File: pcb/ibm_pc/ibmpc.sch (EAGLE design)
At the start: 47 parts, among them IC1 STM32F072C8T6, SW1 324_SW, SW2 324_SW, U1 MAX3232

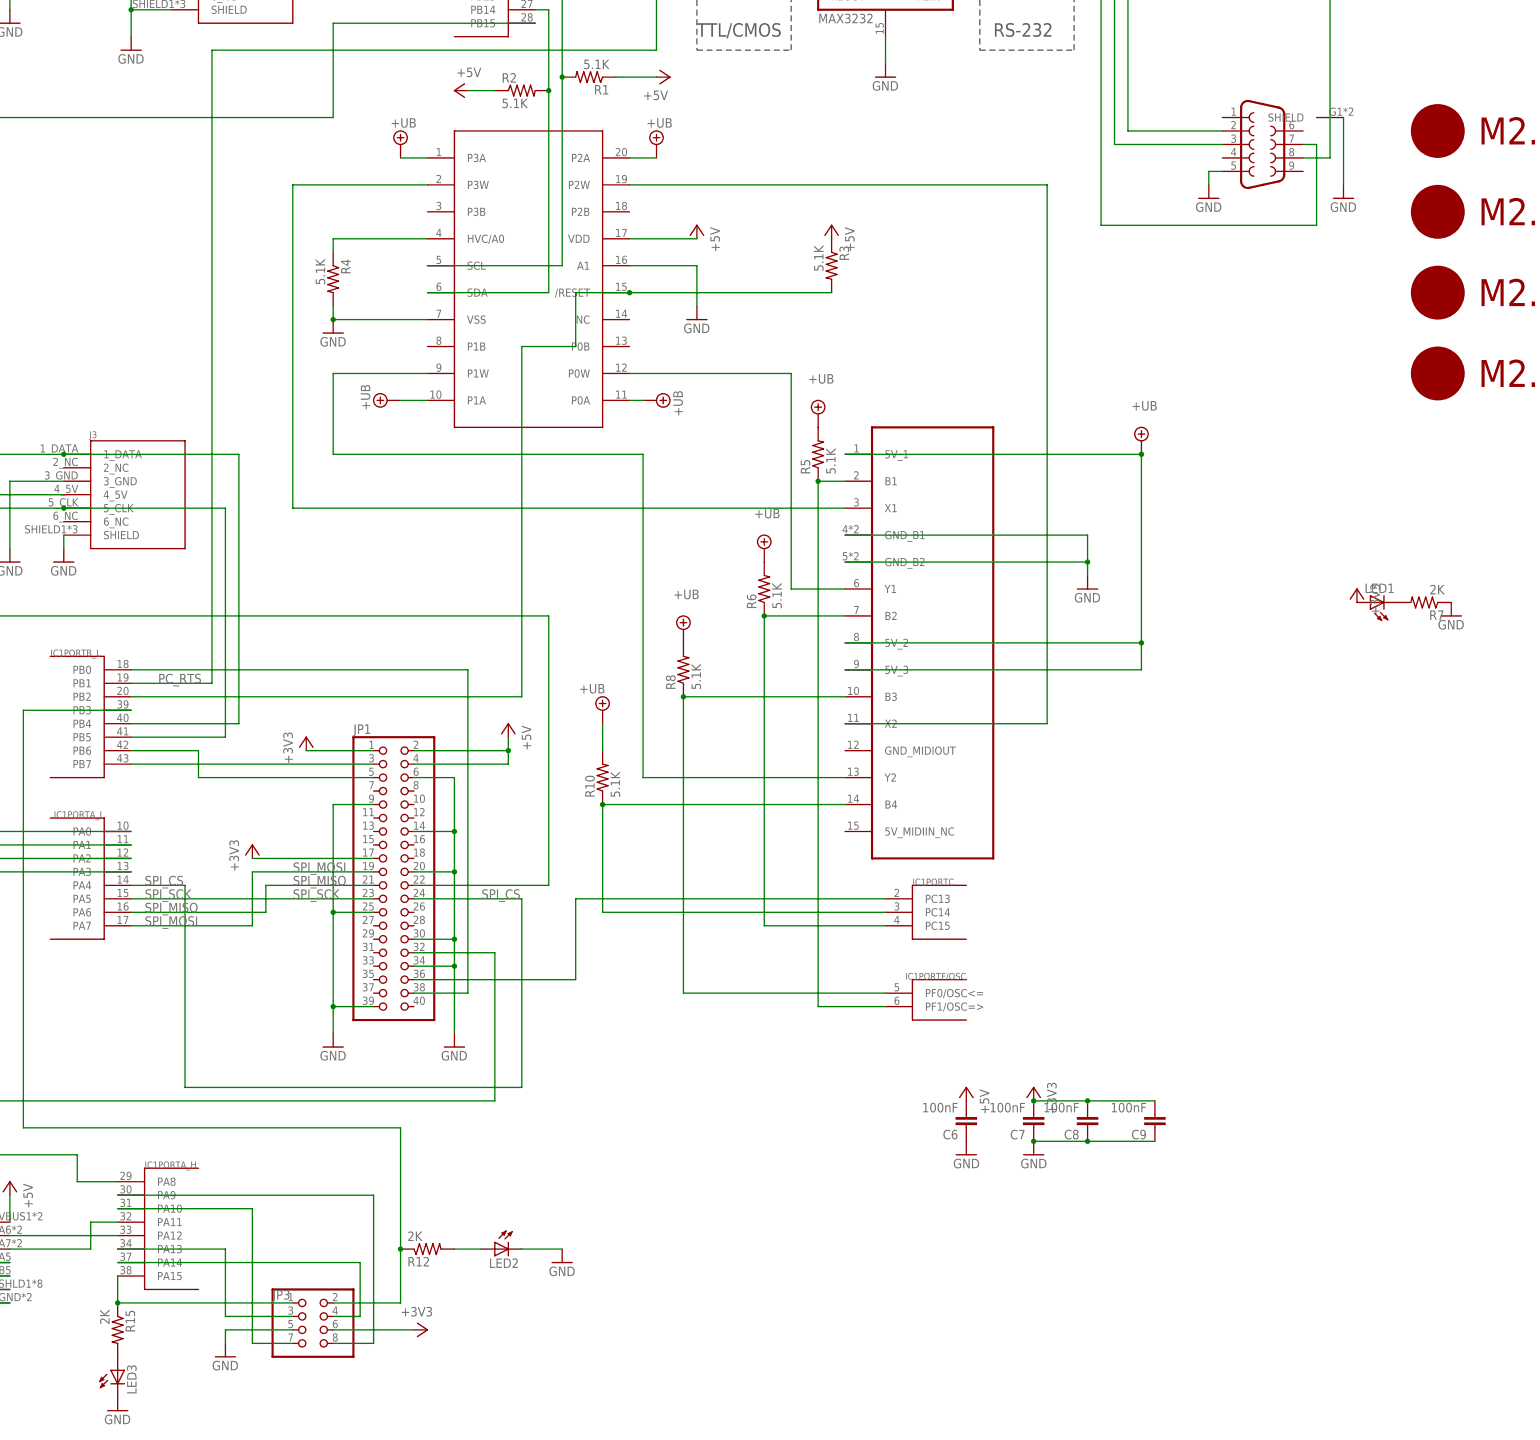
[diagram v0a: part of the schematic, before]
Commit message: added resistor to digipot
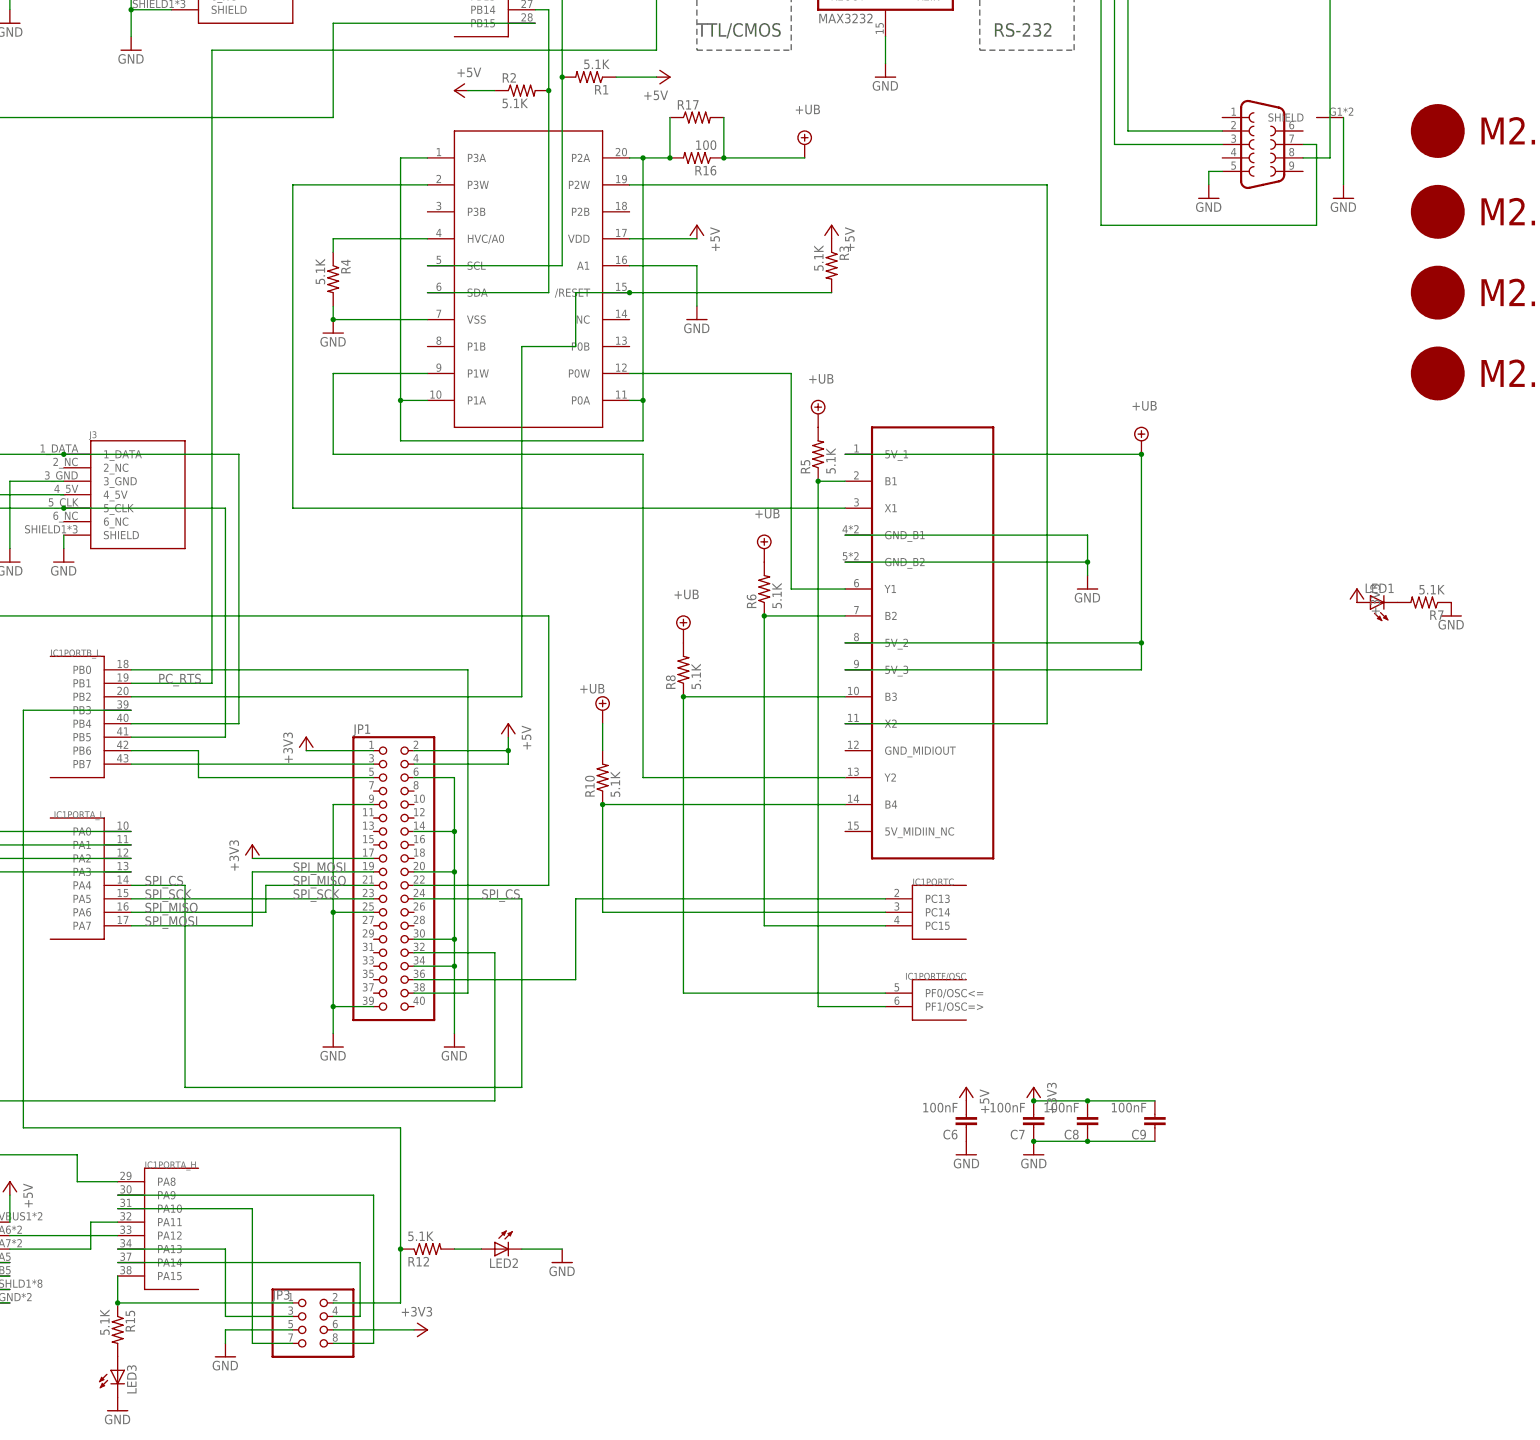
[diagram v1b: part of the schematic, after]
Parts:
- added R16: 100, SparkFun-Passives:RESISTOR0805-RES
- added R17: (no value), adafruit:R-US_0204/7
- R12, R15, R7: value 2K -> 5.1K
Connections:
- new net N$17: R16.2, R17.1, U$5.P0A, U$5.P1A, U$5.P2A, U$5.P3A
- net +UB: now also R16.1, R17.2; no longer U$5.P0A, U$5.P1A, U$5.P2A, U$5.P3A
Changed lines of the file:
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@@
 <part name="+3V16" library="backplane" deviceset="+3V3" device=""/>
 <part name="LED1" library="adafruit" deviceset="LED" device="CHIP-LED0805"/>
-<part name="R7" library="SparkFun-Passives" deviceset="RESISTOR" device="0805-RES" value="2K"/>
+<part name="R7" library="SparkFun-Passives" deviceset="RESISTOR" device="0805-RES" value="5.1K"/>
 <part name="GND9" library="backplane" deviceset="GND" device=""/>
 <part name="C7" library="clock" deviceset="CAP" device="0805" value="100nF"/>
@@
 <part name="GND10" library="backplane" deviceset="GND" device=""/>
 <part name="LED2" library="adafruit" deviceset="LED" device="CHIP-LED0805"/>
-<part name="R12" library="SparkFun-Passives" deviceset="RESISTOR" device="0805-RES" value="2K"/>
+<part name="R12" library="SparkFun-Passives" deviceset="RESISTOR" device="0805-RES" value="5.1K"/>
 <part name="GND13" library="SparkFun-Aesthetics" deviceset="GND" device=""/>
 <part name="U1" library="SparkFun-DigitalIC" deviceset="MAX232" device="SOIC16" value="MAX3232">
@@
 <part name="GND20" library="backplane" deviceset="GND" device=""/>
 <part name="LED3" library="adafruit" deviceset="LED" device="CHIP-LED0805"/>
-<part name="R15" library="SparkFun-Passives" deviceset="RESISTOR" device="0805-RES" value="2K"/>
+<part name="R15" library="SparkFun-Passives" deviceset="RESISTOR" device="0805-RES" value="5.1K"/>
 <part name="GND21" library="supply1" library_urn="urn:adsk.eagle:library:371" deviceset="GND" device=""/>
 <part name="GND22" library="supply1" library_urn="urn:adsk.eagle:library:371" deviceset="GND" device=""/>
@@
 <part name="GND24" library="supply1" library_urn="urn:adsk.eagle:library:371" deviceset="GND" device=""/>
 <part name="R4" library="SparkFun-Passives" deviceset="RESISTOR" device="0805-RES" value="5.1K"/>
-<part name="SUPPLY6" library="supply2" library_urn="urn:adsk.eagle:library:372" deviceset="+UB" device=""/>
-<part name="SUPPLY7" library="supply2" library_urn="urn:adsk.eagle:library:372" deviceset="+UB" device=""/>
-<part name="SUPPLY8" library="supply2" library_urn="urn:adsk.eagle:library:372" deviceset="+UB" device=""/>
-<part name="SUPPLY9" library="supply2" library_urn="urn:adsk.eagle:library:372" deviceset="+UB" device=""/>
 <part name="GND25" library="backplane" deviceset="GND" device=""/>
 <part name="U$10" library="adafruit_changed" deviceset="PINHD1X4" device=""/>
@@
 <part name="GND26" library="supply1" deviceset="GND" device=""/>
 <part name="P+8" library="supply1" library_urn="urn:adsk.eagle:library:371" deviceset="+5V" device=""/>
+<part name="SUPPLY6" library="supply2" library_urn="urn:adsk.eagle:library:372" deviceset="+UB" device=""/>
+<part name="R16" library="SparkFun-Passives" deviceset="RESISTOR" device="0805-RES" value="100"/>
+<part name="R17" library="adafruit" deviceset="R-US_" device="0204/7"/>
 </parts>
 <sheets>
@@
 <attribute name="VALUE" x="77.978" y="135.89" size="1.778" layer="96" rot="R270"/>
 </instance>
-<instance part="SUPPLY6" gate="G$1" x="142.24" y="157.48" smashed="yes">
-<attribute name="VALUE" x="140.335" y="160.655" size="1.778" layer="96"/>
-</instance>
-<instance part="SUPPLY7" gate="G$1" x="93.98" y="157.48" smashed="yes">
-<attribute name="VALUE" x="92.075" y="160.655" size="1.778" layer="96"/>
-</instance>
-<instance part="SUPPLY8" gate="G$1" x="91.44" y="109.22" smashed="yes" rot="R90">
-<attribute name="VALUE" x="88.265" y="107.315" size="1.778" layer="96" rot="R90"/>
-</instance>
-<instance part="SUPPLY9" gate="G$1" x="142.24" y="109.22" smashed="yes" rot="R270">
-<attribute name="VALUE" x="145.415" y="111.125" size="1.778" layer="96" rot="R270"/>
-</instance>
 <instance part="GND25" gate="1" x="20.32" y="78.74" smashed="yes">
 <attribute name="VALUE" x="17.78" y="76.2" size="1.778" layer="96"/>
@@
 <instance part="P+8" gate="1" x="200.66" y="-20.32" smashed="yes" rot="MR0">
 <attribute name="VALUE" x="203.2" y="-25.4" size="1.778" layer="96" rot="MR90"/>
+</instance>
+<instance part="SUPPLY6" gate="G$1" x="170.18" y="157.48" smashed="yes">
+<attribute name="VALUE" x="168.275" y="163.195" size="1.778" layer="96"/>
+</instance>
+<instance part="R16" gate="G$1" x="149.86" y="154.94" smashed="yes" rot="R180">
+<attribute name="NAME" x="153.67" y="153.4414" size="1.778" layer="95" rot="R180"/>
+<attribute name="VALUE" x="153.67" y="158.242" size="1.778" layer="96" rot="R180"/>
+</instance>
+<instance part="R17" gate="G$1" x="149.86" y="162.56" smashed="yes">
+<attribute name="NAME" x="146.05" y="164.0586" size="1.778" layer="95"/>
+<attribute name="VALUE" x="146.05" y="159.258" size="1.778" layer="96"/>
 </instance>
 </instances>
@@
 </segment>
 <segment>
-<pinref part="SUPPLY7" gate="G$1" pin="+UB"/>
-<pinref part="U$5" gate="G$1" pin="P3A"/>
-<wire x1="93.98" y1="154.94" x2="99.06" y2="154.94" width="0.1524" layer="91"/>
-</segment>
-<segment>
+<pinref part="R16" gate="G$1" pin="1"/>
 <pinref part="SUPPLY6" gate="G$1" pin="+UB"/>
-<pinref part="U$5" gate="G$1" pin="P2A"/>
-<wire x1="142.24" y1="154.94" x2="137.16" y2="154.94" width="0.1524" layer="91"/>
-</segment>
-<segment>
-<pinref part="SUPPLY8" gate="G$1" pin="+UB"/>
-<pinref part="U$5" gate="G$1" pin="P1A"/>
-<wire x1="93.98" y1="109.22" x2="99.06" y2="109.22" width="0.1524" layer="91"/>
-</segment>
-<segment>
-<pinref part="U$5" gate="G$1" pin="P0A"/>
-<pinref part="SUPPLY9" gate="G$1" pin="+UB"/>
-<wire x1="137.16" y1="109.22" x2="139.7" y2="109.22" width="0.1524" layer="91"/>
+<wire x1="154.94" y1="154.94" x2="170.18" y2="154.94" width="0.1524" layer="91"/>
+<pinref part="R17" gate="G$1" pin="2"/>
+<wire x1="154.94" y1="162.56" x2="154.94" y2="154.94" width="0.1524" layer="91"/>
+<junction x="154.94" y="154.94"/>
 </segment>
 </net>
@@
 </segment>
 </net>
+<net name="N$17" class="0">
+<segment>
+<pinref part="U$5" gate="G$1" pin="P3A"/>
+<wire x1="93.98" y1="154.94" x2="99.06" y2="154.94" width="0.1524" layer="91"/>
+<pinref part="U$5" gate="G$1" pin="P1A"/>
+<wire x1="93.98" y1="109.22" x2="99.06" y2="109.22" width="0.1524" layer="91"/>
+<wire x1="93.98" y1="154.94" x2="93.98" y2="109.22" width="0.1524" layer="91"/>
+<wire x1="93.98" y1="109.22" x2="93.98" y2="101.6" width="0.1524" layer="91"/>
+<wire x1="93.98" y1="101.6" x2="139.7" y2="101.6" width="0.1524" layer="91"/>
+<junction x="93.98" y="109.22"/>
+<pinref part="U$5" gate="G$1" pin="P0A"/>
+<wire x1="137.16" y1="109.22" x2="139.7" y2="109.22" width="0.1524" layer="91"/>
+<wire x1="139.7" y1="101.6" x2="139.7" y2="109.22" width="0.1524" layer="91"/>
+<pinref part="U$5" gate="G$1" pin="P2A"/>
+<wire x1="139.7" y1="154.94" x2="137.16" y2="154.94" width="0.1524" layer="91"/>
+<wire x1="139.7" y1="109.22" x2="139.7" y2="154.94" width="0.1524" layer="91"/>
+<junction x="139.7" y="109.22"/>
+<junction x="139.7" y="154.94"/>
+<pinref part="R16" gate="G$1" pin="2"/>
+<wire x1="139.7" y1="154.94" x2="144.78" y2="154.94" width="0.1524" layer="91"/>
+<pinref part="R17" gate="G$1" pin="1"/>
+<wire x1="144.78" y1="162.56" x2="144.78" y2="154.94" width="0.1524" layer="91"/>
+<junction x="144.78" y="154.94"/>
+</segment>
+</net>
